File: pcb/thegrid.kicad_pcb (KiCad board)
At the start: 2 copper layers, 50.3 x 100.6 mm, 50 parts, among them P1 POWER, P10 CONN_2, P2 SHIFT_IN, P3 SHIFT_OUT, P4 CONN_2, P5 CONN_2, P6 CONN_2, P7 CONN_2, P8 CONN_2, P9 CONN_2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

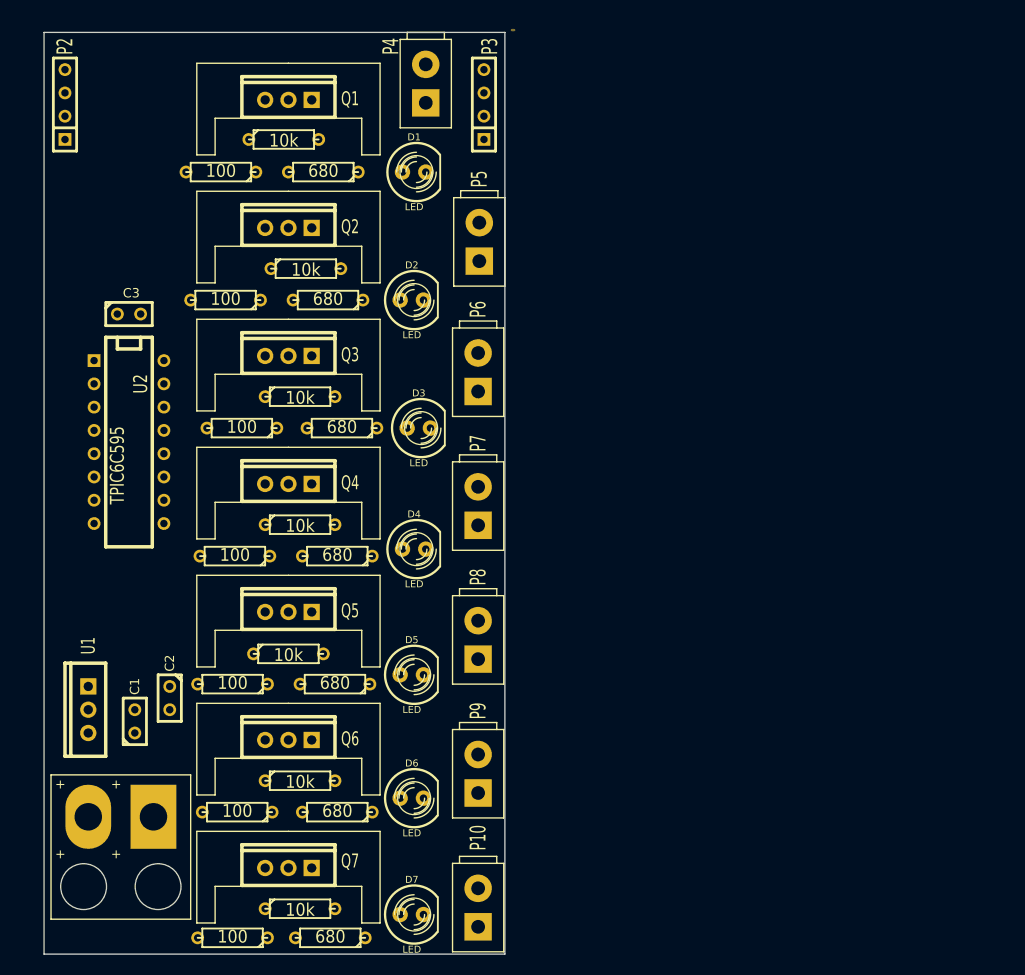
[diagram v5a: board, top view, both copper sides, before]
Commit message: Provisionally finished routing
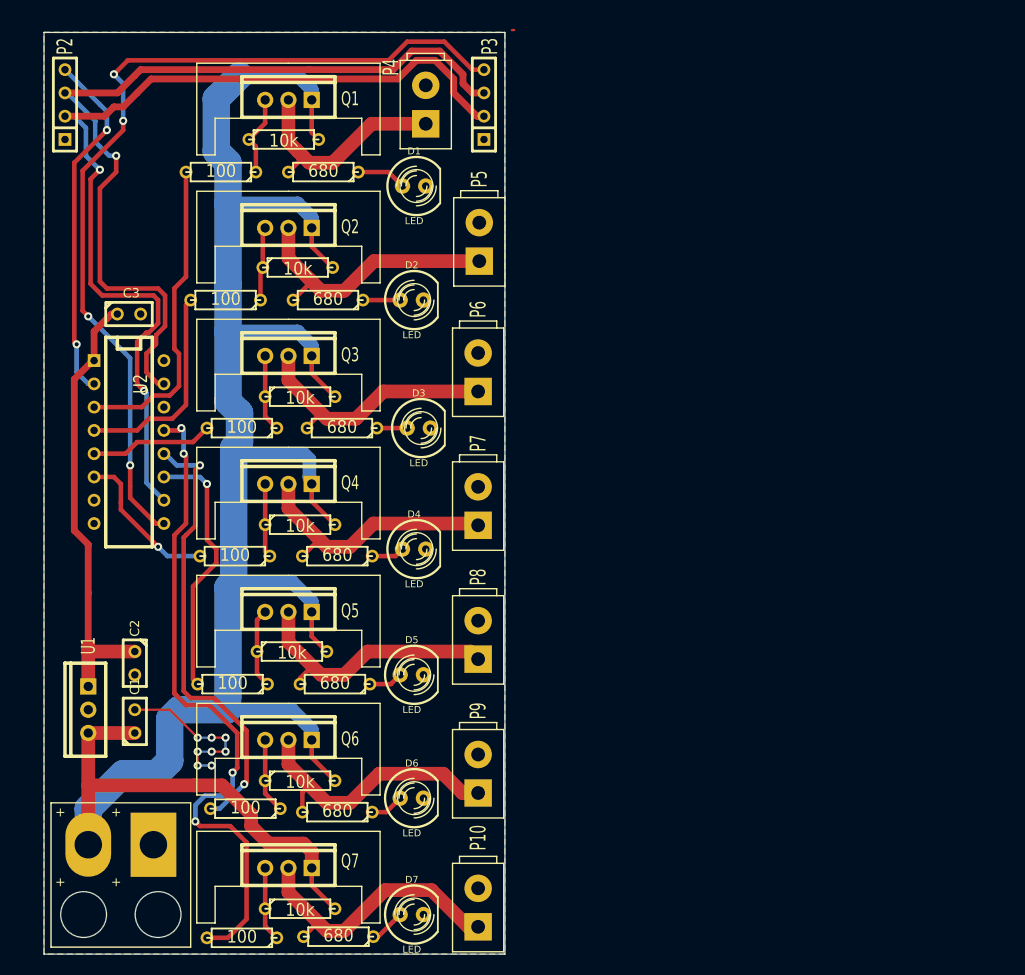
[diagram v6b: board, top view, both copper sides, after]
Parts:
- moved C2 5.39 mm to (130.8, 87.6)
- moved P1 3.05 mm to (129.3, 108.5)
- moved P4 2.29 mm to (162.6, 26.7)
- moved D1 1.52 mm to (161.3, 35.6)
- moved R12 1.02 mm to (142.5, 117.6)
- moved R10 0.97 mm to (142.9, 103.5)
- moved R21 0.90 mm to (153.0, 117.5)
- moved R3 0.90 mm to (148.6, 44.5)
- moved R13 0.46 mm to (148.0, 86.4)
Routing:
- net +12V: track 0.00 -> 245.4 mm
- net Net-(P2-Pad2): track 0.00 -> 104.8 mm, vias 0 -> 2
- net Net-(P3-Pad4): track 0.00 -> 98.6 mm, vias 0 -> 4
- net Net-(P2-Pad3): track 0.00 -> 93.7 mm, vias 0 -> 1
- net Net-(R12-Pad2): track 0.00 -> 73.1 mm, vias 0 -> 4
- net +5V: track 0.00 -> 50.6 mm
- net Net-(R10-Pad2): track 0.00 -> 49.2 mm, vias 0 -> 2
- net Net-(P2-Pad4): track 0.00 -> 38.9 mm, vias 0 -> 2
- net Net-(R2-Pad2): track 0.00 -> 34.3 mm
- net Net-(P10-Pad1): track 0.00 -> 32.8 mm
- net Net-(P5-Pad1): track 0.00 -> 30.7 mm
- net Net-(P9-Pad1): track 0.00 -> 30.5 mm
- net Net-(P7-Pad1): track 0.00 -> 29.6 mm
- net Net-(P8-Pad1): track 0.00 -> 29.4 mm
- net Net-(P6-Pad1): track 0.00 -> 28.6 mm
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- added copper zone on B.Cu, net GND
- added copper zone on F.Cu, net GND
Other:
- net class 1A added: clearance 0.254, trace_width 1.5, via_dia 0.889, via_drill 0.635
- net class 7A added: clearance 0.254, trace_width 4, via_dia 0.889, via_drill 0.635
- net class Logic added: clearance 0.254, trace_width 0.254, via_dia 0.889, via_drill 0.635

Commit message: Made edges of board fit in 100mm x 50mm
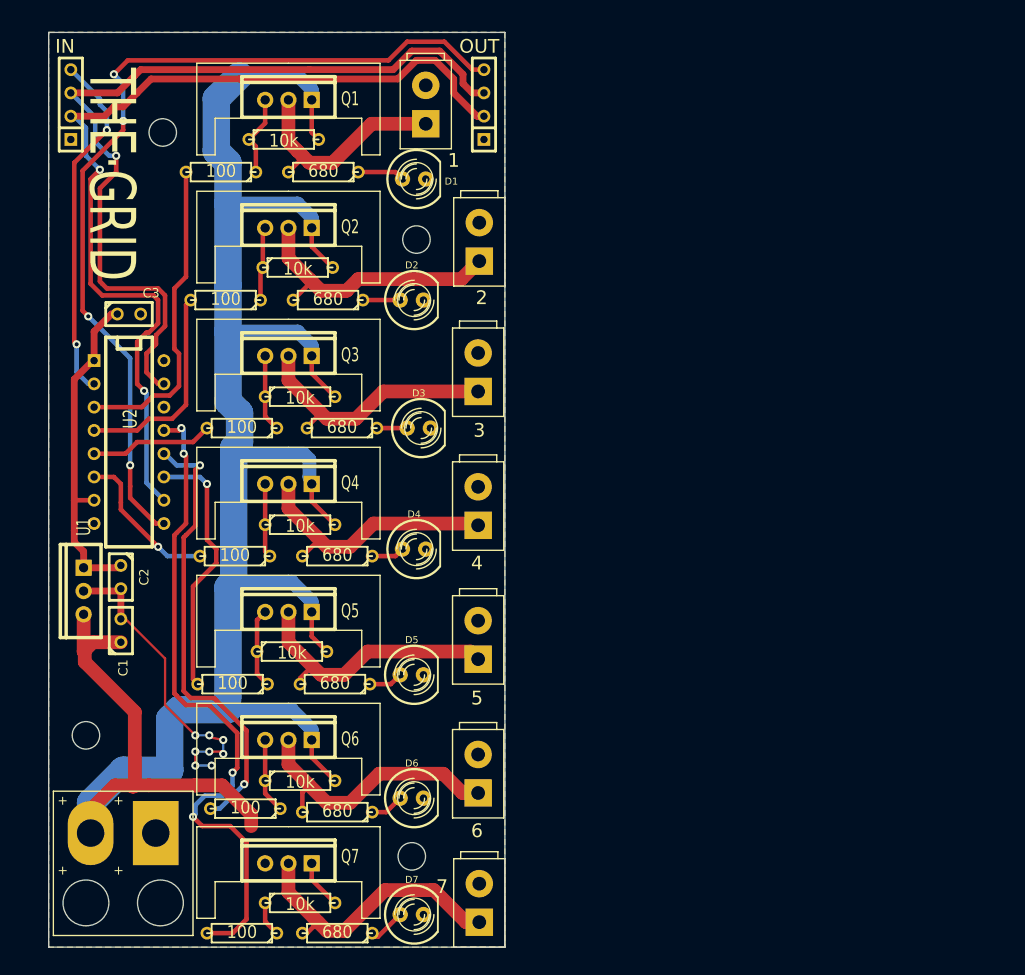
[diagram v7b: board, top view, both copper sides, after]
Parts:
- added MH: MountingHole_3mm_RevA_Date21Jun2010, Mounting_Holes:MountingHole_3mm, F.Cu at (133.9, 29.7)
- added MH: MountingHole_3mm_RevA_Date21Jun2010, Mounting_Holes:MountingHole_3mm, F.Cu at (125.5, 95.5)
- added MH: MountingHole_3mm_RevA_Date21Jun2010, Mounting_Holes:MountingHole_3mm, F.Cu at (161.0, 108.7)
- added MH: MountingHole_3mm_RevA_Date21Jun2010, Mounting_Holes:MountingHole_3mm, F.Cu at (161.5, 41.4)
- moved U1 13.0 mm to (125.2, 79.8)
- moved C1 10.0 mm to (129.3, 84.1)
- moved C2 9.52 mm to (129.3, 78.2)
- moved P1 1.30 mm to (129.5, 107.2)
- moved D1 0.76 mm to (161.3, 34.8)
- moved P2 0.64 mm to (123.8, 26.7)
- moved R11 0.64 mm to (148.8, 113.8)
- moved P10 0.52 mm to (168.4, 113.8)
- moved R12 0.51 mm to (142.5, 117.1)
- moved Q7 0.51 mm to (147.6, 109.5)
- moved R21 0.40 mm to (152.9, 117.1)
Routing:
- net GND: track 18.8 -> 35.0 mm
- net +5V: track 50.6 -> 36.8 mm
- net +12V: track 245.4 -> 251.0 mm
- net Net-(Q7-Pad2): track 8.15 -> 3.83 mm
- net Net-(P2-Pad2): track 104.8 -> 103.5 mm
- net Net-(P2-Pad3): track 93.7 -> 92.7 mm
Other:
- board size 50.3 x 100.6 mm -> 49.8 x 99.8 mm
- board text added: "1"
- board text added: "2"
- board text added: "3"
- board text added: "4"
- board text added: "4 DATA 3 SRCK 2 RCK 1 GND"
- board text added: "5"
- board text added: "6"
- board text added: "7"
- board text added: "ADAM GREIG"
- board text added: "DAVID TURNER"
- board text added: "IN"
- board text added: "OUT"
- board text added: "THE·GRID"

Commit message: Gerbils!
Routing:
- net +12V: track 251.0 -> 260.3 mm
- net Net-(Q7-Pad2): track 3.83 -> 8.15 mm
